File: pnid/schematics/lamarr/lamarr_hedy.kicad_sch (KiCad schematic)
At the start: 81 parts

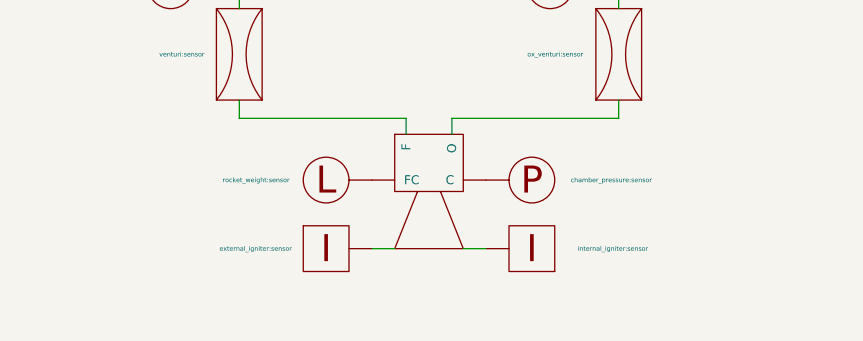
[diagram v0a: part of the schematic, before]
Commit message: update pnids, add main lora pnid, fix camera config
fix some minor issues in pnid state names (igniters)
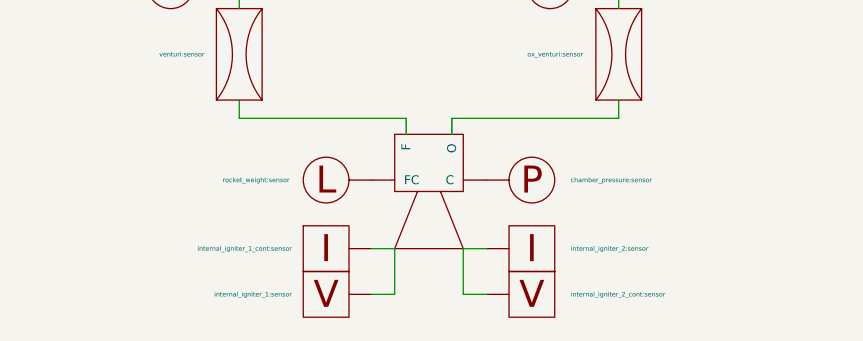
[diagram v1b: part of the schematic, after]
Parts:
- added voltmeter1: internal_igniter_1:sensor, symbol PnID-Lib:voltmeter
- added voltmeter2: internal_igniter_2_cont:sensor, symbol PnID-Lib:voltmeter
- igniter1: value external_igniter:sensor -> internal_igniter_1_cont:sensor
- igniter2: value internal_igniter:sensor -> internal_igniter_2:sensor
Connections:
- net at engine.~ (O): now also venturi1.~; no longer ox_venturi.~
- net at venturi1.~: now also fuel_main_valve.~, fuel_venturi_pressure.~; no longer engine.~ (O)
- net at dewar_needle_valve?.~: now also C2.~, C3.~; no longer C1.~
- net at igniter1.~: now also voltmeter1.~
- net at igniter2.~: now also voltmeter2.~
- net at Orifice2.~: now also fuel_pressurant_valve.~, pressurantPressureRegulator1.~
- new net: engine.~ (O), ox_venturi.~
- new net: OX.~, ox_main_valve.~, ox_quick_connect.~
- new net: DewarOverPressureValve?.~, LOX.~, dewar_pressurize_solenoid.~
- new net: C1.~, dewar_needle_valve?.~
- new net: Orifice1.~, ox_pressurant_valve.~, pressurantPressureRegulator2.~
- new net: FUEL.~, fuel_main_valve.~, ox_quick_connect1.~
- now unconnected: Orifice1.~
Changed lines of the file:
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@@
 	(wire
 		(pts
+			(xy 103.378 198.12) (xy 105.918 198.12)
+		)
+		(stroke
+			(width 0)
+			(type default)
+		)
+	)
+	(wire
+		(pts
 			(xy 21.59 67.564) (xy 21.59 72.644)
 		)
@@
 	(wire
 		(pts
+			(xy 95.758 193.04) (xy 95.758 198.12)
+		)
+		(stroke
+			(width 0)
+			(type default)
+		)
+	)
+	(wire
+		(pts
 			(xy 93.218 193.04) (xy 95.758 193.04)
 		)
@@
 	(wire
 		(pts
+			(xy 103.378 193.04) (xy 103.378 198.12)
+		)
+		(stroke
+			(width 0)
+			(type default)
+		)
+	)
+	(wire
+		(pts
 			(xy 229.87 95.25) (xy 226.568 95.25)
 		)
@@
 	(wire
 		(pts
+			(xy 95.758 198.12) (xy 93.218 198.12)
+		)
+		(stroke
+			(width 0)
+			(type default)
+		)
+	)
+	(wire
+		(pts
 			(xy 120.904 147.32) (xy 120.904 151.13)
 		)
@@
 			)
 		)
-		(property "Value" "external_igniter:sensor"
+		(property "Value" "internal_igniter_1_cont:sensor"
 			(at 84.328 193.04 0)
 			(effects
@@
 			)
 		)
-		(property "Value" "internal_igniter:sensor"
-			(at 116.078 193.04 0)
+		(property "Value" "internal_igniter_2:sensor"
+			(at 115.316 193.04 0)
 			(effects
 				(font
@@
 	)
 	(symbol
+		(lib_id "PnID-Lib:voltmeter")
+		(at 88.138 198.12 0)
+		(unit 1)
+		(exclude_from_sim no)
+		(in_bom yes)
+		(on_board yes)
+		(dnp no)
+		(property "Reference" "voltmeter1"
+			(at 83.058 195.834 0)
+			(effects
+				(font
+					(size 0.508 0.508)
+				)
+				(hide yes)
+			)
+		)
+		(property "Value" "internal_igniter_1:sensor"
+			(at 84.328 198.12 0)
+			(effects
+				(font
+					(size 0.508 0.508)
+				)
+				(justify right)
+			)
+		)
+		(property "Footprint" ""
+			(at 88.138 198.12 0)
+			(effects
+				(font
+					(size 1.27 1.27)
+				)
+				(hide yes)
+			)
+		)
+		(property "Datasheet" ""
+			(at 88.138 198.12 0)
+			(effects
+				(font
+					(size 1.27 1.27)
+				)
+				(hide yes)
+			)
+		)
+		(property "Description" ""
+			(at 88.138 198.12 0)
+			(effects
+				(font
+					(size 1.27 1.27)
+				)
+				(hide yes)
+			)
+		)
+		(property "Unit" "V"
+			(at 88.138 198.12 0)
+			(effects
+				(font
+					(size 1.27 1.27)
+				)
+				(hide yes)
+			)
+		)
+		(pin "~"
+		)
+		(instances
+			(project ""
+				(path "/604fc9f3-63a6-4133-afd1-4a5c2507dc1d"
+					(reference "voltmeter1")
+					(unit 1)
+				)
+			)
+		)
+	)
+	(symbol
 		(lib_id "PnID-Lib:heater")
 		(at 163.83 49.784 0)
@@
 	)
 	(symbol
+		(lib_id "PnID-Lib:voltmeter")
+		(at 110.998 198.12 0)
+		(mirror y)
+		(unit 1)
+		(exclude_from_sim no)
+		(in_bom yes)
+		(on_board yes)
+		(dnp no)
+		(property "Reference" "voltmeter2"
+			(at 116.078 195.834 0)
+			(effects
+				(font
+					(size 0.508 0.508)
+				)
+				(hide yes)
+			)
+		)
+		(property "Value" "internal_igniter_2_cont:sensor"
+			(at 115.316 198.12 0)
+			(effects
+				(font
+					(size 0.508 0.508)
+				)
+				(justify right)
+			)
+		)
+		(property "Footprint" ""
+			(at 110.998 198.12 0)
+			(effects
+				(font
+					(size 1.27 1.27)
+				)
+				(hide yes)
+			)
+		)
+		(property "Datasheet" ""
+			(at 110.998 198.12 0)
+			(effects
+				(font
+					(size 1.27 1.27)
+				)
+				(hide yes)
+			)
+		)
+		(property "Description" ""
+			(at 110.998 198.12 0)
+			(effects
+				(font
+					(size 1.27 1.27)
+				)
+				(hide yes)
+			)
+		)
+		(property "Unit" "V"
+			(at 110.998 198.12 0)
+			(effects
+				(font
+					(size 1.27 1.27)
+				)
+				(hide yes)
+			)
+		)
+		(pin "~"
+		)
+		(instances
+			(project "lamarr_hedy"
+				(path "/604fc9f3-63a6-4133-afd1-4a5c2507dc1d"
+					(reference "voltmeter2")
+					(unit 1)
+				)
+			)
+		)
+	)
+	(symbol
 		(lib_id "PnID-Lib:Valve_Servo")
 		(at 120.904 82.55 90)
@@
 	)
 	(symbol
-		(lib_name "PnID-Lib:Orifice")
 		(lib_id "PnID-Lib:Orifice")
 		(at 112.268 74.676 0)

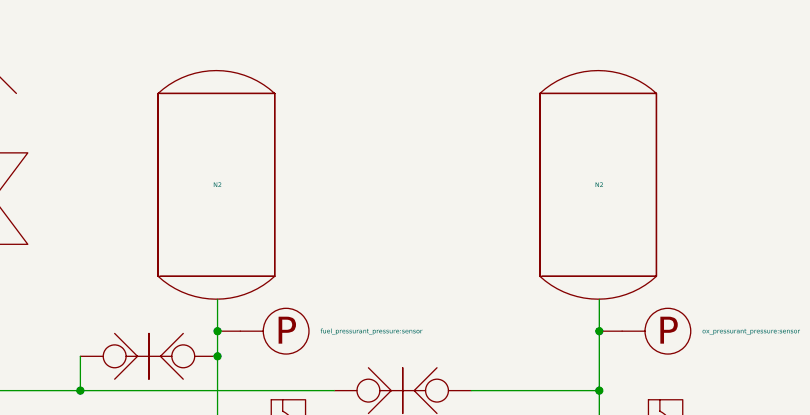
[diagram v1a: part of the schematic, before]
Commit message: update mappings, pnid config, pnids & sequences
- mappings: add slopes to all pi controllers, fix holddown command
- pnid conf: set custom threshold for dewar pressurize valve
  revert holddown config to not use _feedback
  fix state machines formatting
- sequences: load_parameters set to load ox main valve PI parameters
  abort sequence updated to newest system state

also changed influx port due to weird bug in seemingly router firmware
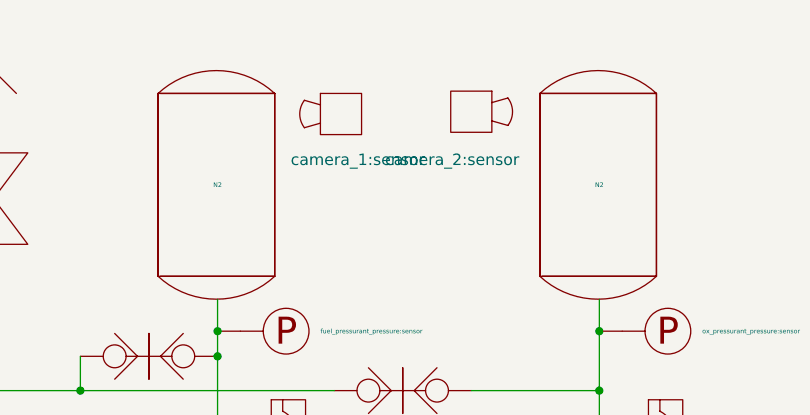
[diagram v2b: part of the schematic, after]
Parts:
- added C6: camera_2:sensor, symbol PnID-Lib:Camera
- added C7: camera_1:sensor, symbol PnID-Lib:Camera
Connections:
- net at engine.~ (O): now also venturi1.~; no longer ox_venturi.~
- net at venturi1.~: now also fuel_main_valve.~, fuel_venturi_pressure.~; no longer engine.~ (O)
- net at dewar_needle_valve?.~: now also C2.~, C3.~; no longer C1.~
- net at Orifice2.~: now also fuel_pressurant_valve.~, pressurantPressureRegulator1.~
- new net: engine.~ (O), ox_venturi.~
- new net: OX.~, ox_main_valve.~, ox_quick_connect.~
- new net: DewarOverPressureValve?.~, LOX.~, dewar_pressurize_solenoid.~
- new net: C1.~, dewar_needle_valve?.~
- new net: Orifice1.~, ox_pressurant_valve.~, pressurantPressureRegulator2.~
- new net: FUEL.~, fuel_main_valve.~, ox_quick_connect1.~
- now unconnected: Orifice1.~
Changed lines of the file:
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@@
+	)
+	(symbol
+		(lib_id "PnID-Lib:Camera")
+		(at 106.68 25.146 0)
+		(unit 1)
+		(exclude_from_sim no)
+		(in_bom yes)
+		(on_board yes)
+		(dnp no)
+		(property "Reference" "C6"
+			(at 106.68 19.304 0)
+			(effects
+				(font
+					(size 1.27 1.27)
+				)
+				(hide yes)
+			)
+		)
+		(property "Value" "camera_2:sensor"
+			(at 112.014 30.48 0)
+			(effects
+				(font
+					(size 1.27 1.27)
+				)
+				(justify right)
+			)
+		)
+		(property "Footprint" ""
+			(at 107.442 21.336 0)
+			(effects
+				(font
+					(size 1.27 1.27)
+				)
+				(hide yes)
+			)
+		)
+		(property "Datasheet" ""
+			(at 107.442 21.336 0)
+			(effects
+				(font
+					(size 1.27 1.27)
+				)
+				(hide yes)
+			)
+		)
+		(property "Description" ""
+			(at 106.68 25.146 0)
+			(effects
+				(font
+					(size 1.27 1.27)
+				)
+				(hide yes)
+			)
+		)
+		(instances
+			(project ""
+				(path "/604fc9f3-63a6-4133-afd1-4a5c2507dc1d"
+					(reference "C6")
+					(unit 1)
+				)
+			)
+		)
 	)
 	(symbol
@@
 					(unit 1)
 				)
+			)
+		)
+	)
+	(symbol
+		(lib_id "PnID-Lib:Camera")
+		(at 92.202 25.4 0)
+		(mirror y)
+		(unit 1)
+		(exclude_from_sim no)
+		(in_bom yes)
+		(on_board yes)
+		(dnp no)
+		(property "Reference" "C7"
+			(at 92.202 19.558 0)
+			(effects
+				(font
+					(size 1.27 1.27)
+				)
+				(hide yes)
+			)
+		)
+		(property "Value" "camera_1:sensor"
+			(at 86.614 30.48 0)
+			(effects
+				(font
+					(size 1.27 1.27)
+				)
+				(justify right)
+			)
+		)
+		(property "Footprint" ""
+			(at 91.44 21.59 0)
+			(effects
+				(font
+					(size 1.27 1.27)
+				)
+				(hide yes)
+			)
+		)
+		(property "Datasheet" ""
+			(at 91.44 21.59 0)
+			(effects
+				(font
+					(size 1.27 1.27)
+				)
+				(hide yes)
+			)
+		)
+		(property "Description" ""
+			(at 92.202 25.4 0)
+			(effects
+				(font
+					(size 1.27 1.27)
+				)
+				(hide yes)
+			)
+		)
+		(instances
+			(project "lamarr_hedy"
+				(path "/604fc9f3-63a6-4133-afd1-4a5c2507dc1d"
+					(reference "C7")
+					(unit 1)
+				)

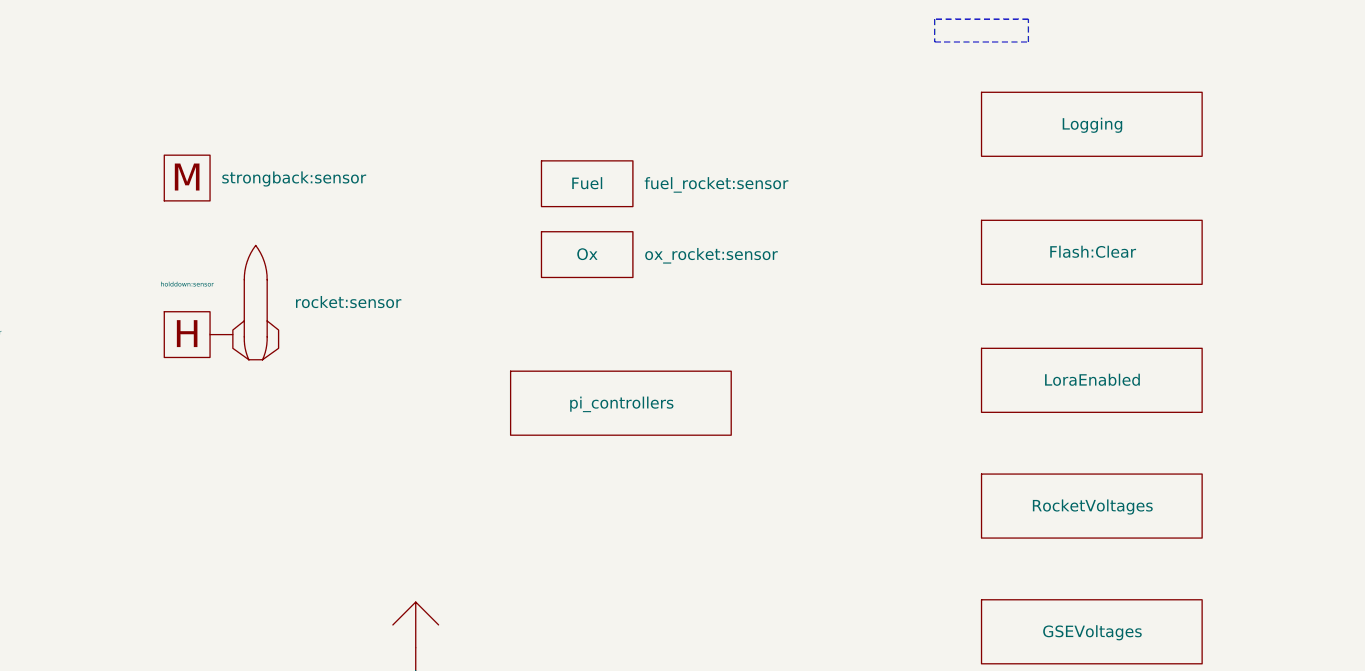
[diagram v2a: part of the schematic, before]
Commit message: various fixes
configure lora use,
fix guidance & navigation pnid,
fix retract threshold
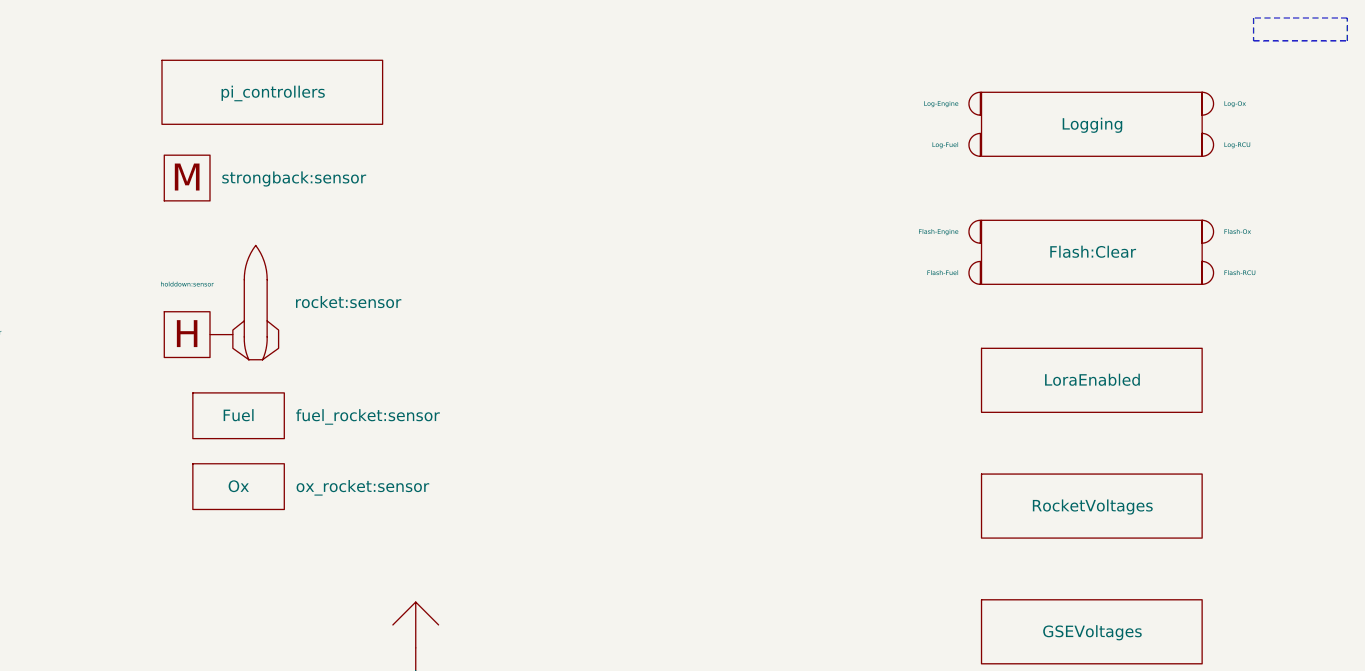
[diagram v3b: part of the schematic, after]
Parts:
- added Flash-Engine: ecu:FlashStatus, symbol PnID-Lib:LED
- added Flash-Fuel: fuel_ecu:FlashStatus, symbol PnID-Lib:LED
- added Flash-Ox: ox_ecu:FlashStatus, symbol PnID-Lib:LED
- added Flash-RCU: rcu:FlashStatus, symbol PnID-Lib:LED
- added Log-Engine: engine_ecu:LoggingEnabled, symbol PnID-Lib:LED
- added Log-Fuel: fuel_ecu:LoggingEnabled, symbol PnID-Lib:LED
- added Log-Ox: ox_ecu:LoggingEnabled, symbol PnID-Lib:LED
- added Log-RCU: rcu:LoggingEnabled, symbol PnID-Lib:LED
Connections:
- net at engine.~ (O): now also venturi1.~; no longer ox_venturi.~
- net at venturi1.~: now also fuel_main_valve.~, fuel_venturi_pressure.~; no longer engine.~ (O)
- net at dewar_needle_valve?.~: now also C2.~, C3.~; no longer C1.~
- net at Orifice2.~: now also fuel_pressurant_valve.~, pressurantPressureRegulator1.~
- new net: engine.~ (O), ox_venturi.~
- new net: OX.~, ox_main_valve.~, ox_quick_connect.~
- new net: DewarOverPressureValve?.~, LOX.~, dewar_pressurize_solenoid.~
- new net: C1.~, dewar_needle_valve?.~
- new net: Orifice1.~, ox_pressurant_valve.~, pressurantPressureRegulator2.~
- new net: FUEL.~, fuel_main_valve.~, ox_quick_connect1.~
- now unconnected: Orifice1.~
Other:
- moved on the sheet: Fuel, Ox

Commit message: i mog schlafn
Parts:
- Flash-Engine: value ecu:FlashStatus -> engine_ecu:FlashStatus
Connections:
- net at engine.~ (O): now also venturi1.~; no longer ox_venturi.~
- net at venturi1.~: now also fuel_main_valve.~, fuel_venturi_pressure.~; no longer engine.~ (O)
- net at dewar_needle_valve?.~: now also C2.~, C3.~; no longer C1.~
- net at Orifice2.~: now also fuel_pressurant_valve.~, pressurantPressureRegulator1.~
- new net: engine.~ (O), ox_venturi.~
- new net: OX.~, ox_main_valve.~, ox_quick_connect.~
- new net: DewarOverPressureValve?.~, LOX.~, dewar_pressurize_solenoid.~
- new net: C1.~, dewar_needle_valve?.~
- new net: Orifice1.~, ox_pressurant_valve.~, pressurantPressureRegulator2.~
- new net: FUEL.~, fuel_main_valve.~, ox_quick_connect1.~
- now unconnected: Orifice1.~
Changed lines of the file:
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@@
 			)
 		)
-		(property "Value" "ecu:FlashStatus"
+		(property "Value" "engine_ecu:FlashStatus"
 			(at 251.46 35.814 90)
 			(effects
